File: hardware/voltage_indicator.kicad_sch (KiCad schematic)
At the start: 15 parts, among them J1 HV+, J2 HV-, U2 LM211DT

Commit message: Improve the layout
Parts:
- added R10: 1k2, Resistor_SMD:R_0603_1608Metric, symbol Device:R_Small
- added TP2: LM_N, TestPoint:TestPoint_Pad_D1.0mm, symbol Connector:TestPoint
- added TP2: LM_OUT, TestPoint:TestPoint_Pad_D1.0mm, symbol Connector:TestPoint
- added TP2: LM_P, TestPoint:TestPoint_Pad_D1.0mm, symbol Connector:TestPoint
- D1: footprint LED_THT:LED_D5.0mm -> LED_THT:LED_Rectangular_W3.9mm_H1.9mm; symbol Device:LED -> Device:LED_Small
- F1: footprint vindicator:01020071Z-FUSE-CLIP -> Local_Library:FuseClip
- J1, J2: footprint Connector_Wire:SolderWire-0.5sqmm_1x01_D0.9mm_OD2.1mm_Relief -> Local_Library:SolderWire_Relief
- R9: renamed from R10; value 240 -> 240R
- renumbered R5 to R11, R6 to R5, R7 to R6, R8 to R7, R9 to R8, U2 to U1
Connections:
- net +12V: now also R10.1
- net at R6.1, R7.2, U1.3 (-): now also TP2.1
- net at R8.1, R9.2, U1.2 (+): now also TP2.1
- net at D1.1 (K), U1.7: now also R10.2, TP2.1
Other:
- note removed: "0.889 V to 9.279 V"
- note removed: "For 54.229 V we get 0.889 V For 566 V we get 9.279 V"
- company: (none) -> H. Fedarovich
- moved on the sheet: D1, F1, J1, J2, R1, R11, R2, R3, R4, R5, R6, R7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

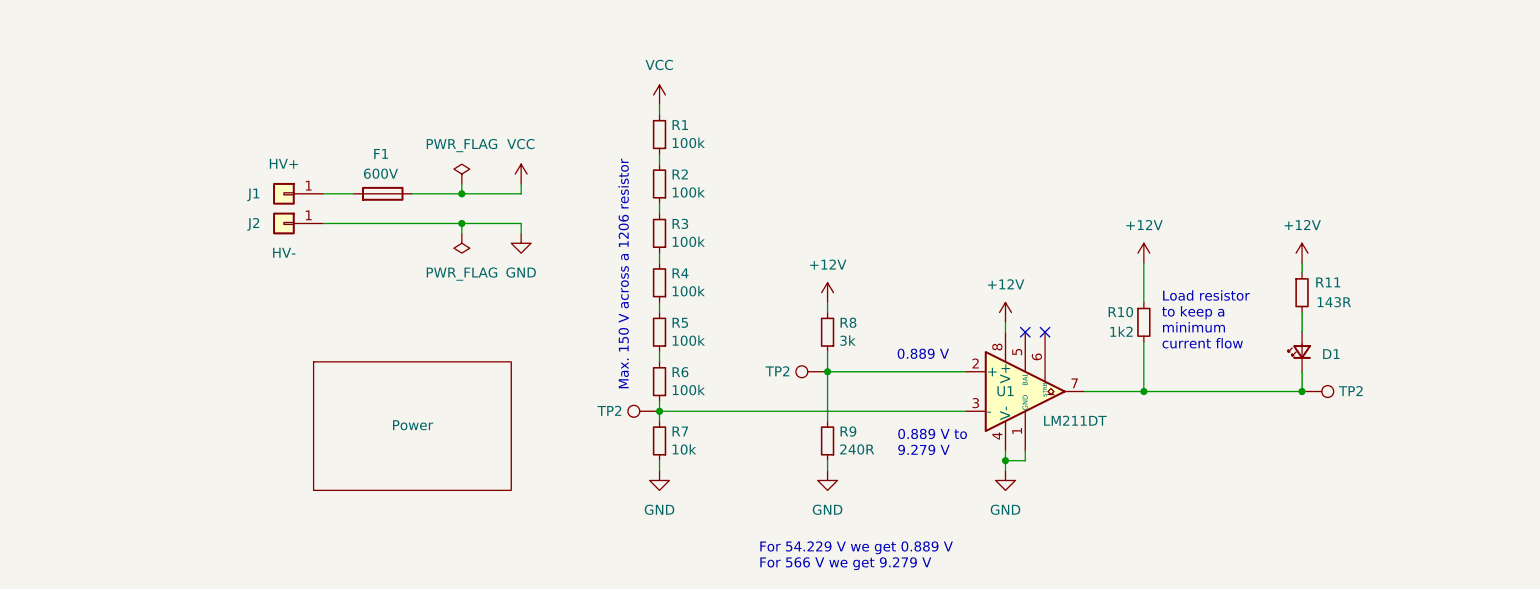
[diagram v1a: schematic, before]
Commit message: Use a transistor to drive the LED
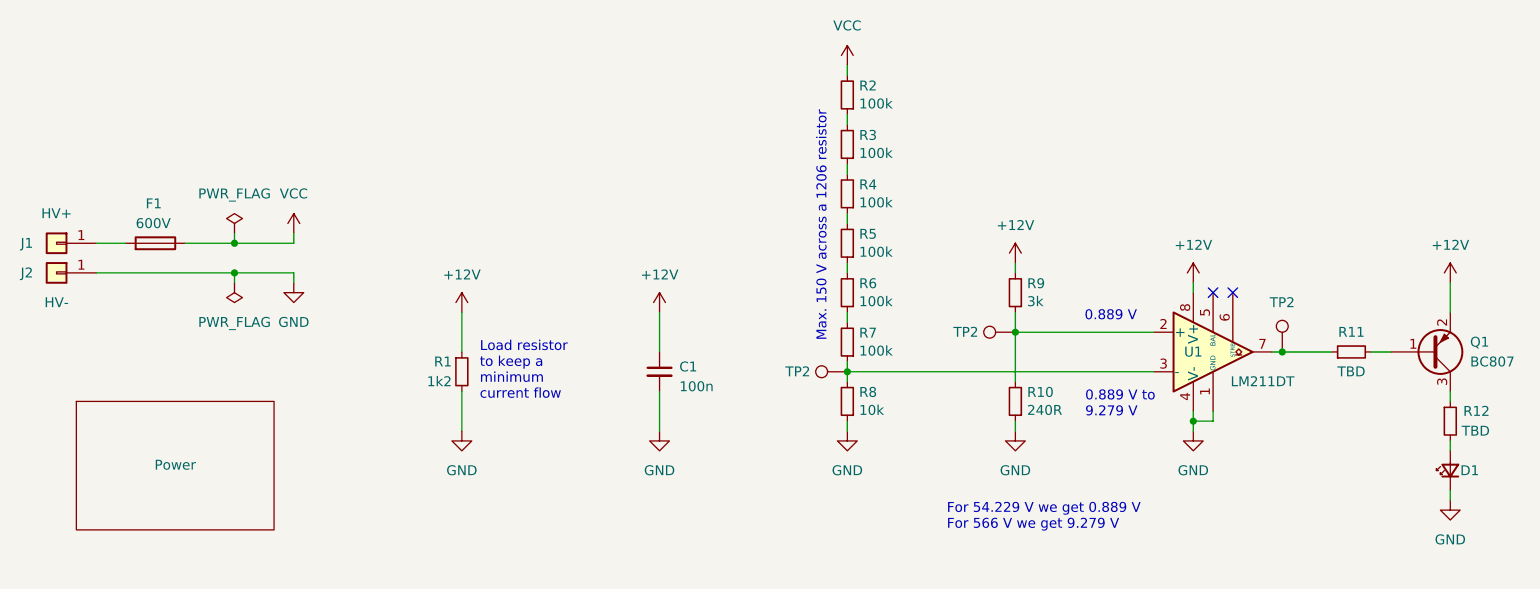
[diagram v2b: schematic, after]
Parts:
- added C1: 100n, Capacitor_SMD:C_0603_1608Metric, symbol Device:C_Small
- added Q1: BC807, Package_TO_SOT_SMD:SOT-23, symbol Transistor_BJT:BC807
- added R12: TBD, Resistor_SMD:R_0603_1608Metric, symbol Device:R_Small
- R11: value 143R -> TBD
- renumbered R10 to R1, R9 to R10, R1 to R2, R2 to R3, R3 to R4, R4 to R5, R5 to R6, R6 to R7, R7 to R8, R8 to R9
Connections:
- net +12V: now also C1.1, Q1.2 (E); no longer R11.1
- net GND: now also D1.1 (K), R1.2, C1.2
- net at TP2.1, U1.7: now also R11.1; no longer D1.1 (K), R1.2
- net at R11.2: now also Q1.1 (B); no longer D1.2 (A)
- new net: Q1.3 (C), R12.1
- new net: D1.2 (A), R12.2
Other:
- moved on the sheet: F1, J1, J2, R1, R10, R2, R3, R4, R5, R6, R7, R8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

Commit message: Update component values
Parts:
- R1: value 1k2 -> 1k
- R11: value TBD -> 1k5
- R12: value TBD -> 470R
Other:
- moved on the sheet: D1, Q1, R11, R12
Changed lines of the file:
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@@
   (no_connect (at 205.74 95.25))
   (no_connect (at 208.28 95.25))
-  (wire (pts (xy 236.22 114.3) (xy 236.22 115.57))
+  (wire (pts (xy 233.68 114.3) (xy 233.68 115.57))
     (stroke (width 0) (type default))
   )
@@
     (stroke (width 0) (type default))
   )
-  (wire (pts (xy 236.22 107.95) (xy 236.22 109.22))
+  (wire (pts (xy 233.68 107.95) (xy 233.68 109.22))
     (stroke (width 0) (type default))
   )
@@
     (stroke (width 0) (type default))
   )
-  (wire (pts (xy 226.06 102.87) (xy 228.6 102.87))
+  (wire (pts (xy 224.79 102.87) (xy 226.06 102.87))
     (stroke (width 0) (type default))
   )
@@
     (stroke (width 0) (type default))
   )
-  (wire (pts (xy 236.22 93.98) (xy 236.22 97.79))
-    (stroke (width 0) (type default))
-  )
-  (wire (pts (xy 236.22 120.65) (xy 236.22 121.92))
+  (wire (pts (xy 233.68 93.98) (xy 233.68 97.79))
+    (stroke (width 0) (type default))
+  )
+  (wire (pts (xy 233.68 120.65) (xy 233.68 121.92))
     (stroke (width 0) (type default))
   )
@@
     (stroke (width 0) (type default))
   )
-  (wire (pts (xy 214.63 102.87) (xy 220.98 102.87))
+  (wire (pts (xy 214.63 102.87) (xy 219.71 102.87))
     (stroke (width 0) (type default))
   )
@@
   )
   (text_box "For 54.229 V we get 0.889 V\nFor 566 V we get 9.279 V"
-    (at 170.4975 121.0531 0) (size 31.4325 5.6294)
+    (at 176.8475 122.3231 0) (size 31.4325 5.6294)
     (stroke (width -0.0001) (type default))
     (fill (type none))
     (effects (font (size 1.27 1.27)) (justify left top))
   )
-  (text_box "0.889 V to 9.279 V"
+  (text_box "0.889 to 9.279 V"
     (at 188.2775 106.6005 0) (size 13.6525 5.1595)
     (stroke (width -0.0001) (type default))
@@
   )
   (text_box "Load resistor to keep a minimum current flow"
-    (at 110.49 100.2505 0) (size 15.24 8.9695)
+    (at 114.3 101.5205 0) (size 15.24 8.9695)
     (stroke (width -0.0001) (type default))
     (fill (type none))
@@
     )
   )
-  (symbol (lib_id "Transistor_BJT:BC807") (at 233.68 102.87 0) (mirror x) (unit 1)
-    (in_bom yes) (on_board yes) (dnp no)
-    (property "Reference" "Q1" (at 238.76 101.6 0)
+  (symbol (lib_id "Transistor_BJT:BC807") (at 231.14 102.87 0) (mirror x) (unit 1)
+    (in_bom yes) (on_board yes) (dnp no)
+    (property "Reference" "Q1" (at 236.22 101.6 0)
       (effects (font (size 1.27 1.27)) (justify left))
     )
-    (property "Value" "BC807" (at 238.76 104.14 0)
+    (property "Value" "BC807" (at 236.22 104.14 0)
       (effects (font (size 1.27 1.27)) (justify left))
     )
-    (property "Footprint" "Package_TO_SOT_SMD:SOT-23" (at 238.76 100.965 0)
+    (property "Footprint" "Package_TO_SOT_SMD:SOT-23" (at 236.22 100.965 0)
       (effects (font (size 1.27 1.27) italic) (justify left) hide)
     )
-    (property "Datasheet" "https://www.onsemi.com/pub/Collateral/BC808-D.pdf" (at 233.68 102.87 0)
+    (property "Datasheet" "https://www.onsemi.com/pub/Collateral/BC808-D.pdf" (at 231.14 102.87 0)
       (effects (font (size 1.27 1.27)) (justify left) hide)
     )
@@
     )
   )
-  (symbol (lib_id "Device:R_Small") (at 223.52 102.87 90) (unit 1)
-    (in_bom yes) (on_board yes) (dnp no)
-    (property "Reference" "R11" (at 223.52 100.33 90)
-      (effects (font (size 1.27 1.27)))
-    )
-    (property "Value" "TBD" (at 223.52 105.41 90)
-      (effects (font (size 1.27 1.27)))
-    )
-    (property "Footprint" "Resistor_SMD:R_0603_1608Metric" (at 223.52 102.87 0)
-      (effects (font (size 1.27 1.27)) hide)
-    )
-    (property "Datasheet" "~" (at 223.52 102.87 0)
+  (symbol (lib_id "Device:R_Small") (at 222.25 102.87 90) (unit 1)
+    (in_bom yes) (on_board yes) (dnp no)
+    (property "Reference" "R11" (at 222.25 100.33 90)
+      (effects (font (size 1.27 1.27)))
+    )
+    (property "Value" "1k5" (at 222.25 105.41 90)
+      (effects (font (size 1.27 1.27)))
+    )
+    (property "Footprint" "Resistor_SMD:R_0603_1608Metric" (at 222.25 102.87 0)
+      (effects (font (size 1.27 1.27)) hide)
+    )
+    (property "Datasheet" "~" (at 222.25 102.87 0)
       (effects (font (size 1.27 1.27)) hide)
     )
@@
     )
   )
-  (symbol (lib_id "Device:R_Small") (at 109.22 105.41 0) (unit 1)
-    (in_bom yes) (on_board yes) (dnp no)
-    (property "Reference" "R1" (at 107.95 104.14 0)
-      (effects (font (size 1.27 1.27)) (justify right))
-    )
-    (property "Value" "1k2" (at 107.95 106.68 0)
+  (symbol (lib_id "Device:R_Small") (at 109.22 105.41 0) (mirror y) (unit 1)
+    (in_bom yes) (on_board yes) (dnp no)
+    (property "Reference" "R1" (at 110.49 104.14 0)
+      (effects (font (size 1.27 1.27)) (justify right))
+    )
+    (property "Value" "1k" (at 110.49 106.68 0)
       (effects (font (size 1.27 1.27)) (justify right))
     )
@@
     )
   )
-  (symbol (lib_id "Device:R_Small") (at 236.22 111.76 0) (unit 1)
-    (in_bom yes) (on_board yes) (dnp no)
-    (property "Reference" "R12" (at 241.3 110.49 0)
-      (effects (font (size 1.27 1.27)) (justify right))
-    )
-    (property "Value" "TBD" (at 241.3 113.03 0)
-      (effects (font (size 1.27 1.27)) (justify right))
-    )
-    (property "Footprint" "Resistor_SMD:R_0603_1608Metric" (at 236.22 111.76 0)
-      (effects (font (size 1.27 1.27)) hide)
-    )
-    (property "Datasheet" "~" (at 236.22 111.76 0)
+  (symbol (lib_id "Device:R_Small") (at 233.68 111.76 0) (unit 1)
+    (in_bom yes) (on_board yes) (dnp no)
+    (property "Reference" "R12" (at 234.95 110.49 0)
+      (effects (font (size 1.27 1.27)) (justify left))
+    )
+    (property "Value" "470R" (at 234.95 113.03 0)
+      (effects (font (size 1.27 1.27)) (justify left))
+    )
+    (property "Footprint" "Resistor_SMD:R_0603_1608Metric" (at 233.68 111.76 0)
+      (effects (font (size 1.27 1.27)) hide)
+    )
+    (property "Datasheet" "~" (at 233.68 111.76 0)
       (effects (font (size 1.27 1.27)) hide)
     )
@@
     )
   )
-  (symbol (lib_id "power:+12V") (at 236.22 93.98 0) (unit 1)
-    (in_bom yes) (on_board yes) (dnp no)
-    (property "Reference" "#PWR013" (at 236.22 97.79 0)
-      (effects (font (size 1.27 1.27)) hide)
-    )
-    (property "Value" "+12V" (at 236.22 89.154 0)
-      (effects (font (size 1.27 1.27)))
-    )
-    (property "Footprint" "" (at 236.22 93.98 0)
-      (effects (font (size 1.27 1.27)) hide)
-    )
-    (property "Datasheet" "" (at 236.22 93.98 0)
+  (symbol (lib_id "power:+12V") (at 233.68 93.98 0) (unit 1)
+    (in_bom yes) (on_board yes) (dnp no)
+    (property "Reference" "#PWR013" (at 233.68 97.79 0)
+      (effects (font (size 1.27 1.27)) hide)
+    )
+    (property "Value" "+12V" (at 233.68 89.154 0)
+      (effects (font (size 1.27 1.27)))
+    )
+    (property "Footprint" "" (at 233.68 93.98 0)
+      (effects (font (size 1.27 1.27)) hide)
+    )
+    (property "Datasheet" "" (at 233.68 93.98 0)
       (effects (font (size 1.27 1.27)) hide)
     )
@@
   (symbol (lib_id "Comparator:LM311") (at 205.74 102.87 0) (unit 1)
     (in_bom yes) (on_board yes) (dnp no)
-    (property "Reference" "U1" (at 203.2 102.87 0)
+    (property "Reference" "U1" (at 199.39 96.52 0)
       (effects (font (size 1.27 1.27)))
     )
@@
     )
   )
-  (symbol (lib_id "power:GND") (at 236.22 121.92 0) (unit 1)
-    (in_bom yes) (on_board yes) (dnp no)
-    (property "Reference" "#PWR014" (at 236.22 128.27 0)
-      (effects (font (size 1.27 1.27)) hide)
-    )
-    (property "Value" "GND" (at 236.22 127 0)
-      (effects (font (size 1.27 1.27)))
-    )
-    (property "Footprint" "" (at 236.22 121.92 0)
-      (effects (font (size 1.27 1.27)) hide)
-    )
-    (property "Datasheet" "" (at 236.22 121.92 0)
+  (symbol (lib_id "power:GND") (at 233.68 121.92 0) (unit 1)
+    (in_bom yes) (on_board yes) (dnp no)
+    (property "Reference" "#PWR014" (at 233.68 128.27 0)
+      (effects (font (size 1.27 1.27)) hide)
+    )
+    (property "Value" "GND" (at 233.68 127 0)
+      (effects (font (size 1.27 1.27)))
+    )
+    (property "Footprint" "" (at 233.68 121.92 0)
+      (effects (font (size 1.27 1.27)) hide)
+    )
+    (property "Datasheet" "" (at 233.68 121.92 0)
       (effects (font (size 1.27 1.27)) hide)
     )
@@
     )
   )
-  (symbol (lib_id "Device:LED_Small") (at 236.22 118.11 90) (unit 1)
-    (in_bom yes) (on_board yes) (dnp no)
-    (property "Reference" "D1" (at 237.49 118.11 90)
-      (effects (font (size 1.27 1.27)) (justify right))
-    )
-    (property "Value" "Red" (at 238.76 119.6974 90)
-      (effects (font (size 1.27 1.27)) (justify right) hide)
-    )
-    (property "Footprint" "LED_THT:LED_Rectangular_W3.9mm_H1.9mm" (at 236.22 118.11 90)
-      (effects (font (size 1.27 1.27)) hide)
-    )
-    (property "Datasheet" "~" (at 236.22 118.11 90)
-      (effects (font (size 1.27 1.27)) hide)
-    )
+  (symbol (lib_id "Device:LED_Small") (at 233.68 118.11 90) (unit 1)
+    (in_bom yes) (on_board yes) (dnp no)
+    (property "Reference" "D1" (at 234.95 116.84 90)
+      (effects (font (size 1.27 1.27)) (justify right))
+    )
+    (property "Value" "Red" (at 234.95 119.6974 90)
+      (effects (font (size 1.27 1.27)) (justify right))
+    )
+    (property "Footprint" "LED_THT:LED_Rectangular_W3.9mm_H1.9mm" (at 233.68 118.11 90)
+      (effects (font (size 1.27 1.27)) hide)
+    )
+    (property "Datasheet" "~" (at 233.68 118.11 90)
+      (effects (font (size 1.27 1.27)) hide)
+    )
